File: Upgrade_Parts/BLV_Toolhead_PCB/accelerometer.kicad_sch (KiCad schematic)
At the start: 8 parts

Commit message: termination fix
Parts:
- added R?: 100, symbol Device:R
- added U?: SN65LVDS1DBV, Package_TO_SOT_SMD:SOT-23-5, symbol Interface:SN65LVDS1DBV
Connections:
- net SPI_MOSI_N: now also R?.2
- net SPI_MOSI_P: now also R?.1
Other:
- note added: "3.3V version SN65LVDS2 missing symbol"
- note added: "5V!!!"
- company: (none) -> https://github.com/Battosai42/CraftbotPlus_Upgrade
- title: (none) -> BLF Toolhaed PCB
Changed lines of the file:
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@@
 (kicad_sch (version 20211123) (generator eeschema)
   (paper "A4")
+  (title_block
+    (title "BLF Toolhaed PCB")
+    (date "2022-07-16")
+    (rev "0.1")
+    (company "https://github.com/Battosai42/CraftbotPlus_Upgrade")
+  )
   (junction (at 143.51 39.37) (diameter 0) (color 0 0 0 0)
   )
@@
   (junction (at 143.51 109.22) (diameter 0) (color 0 0 0 0)
   )
+  (junction (at 97.155 80.01) (diameter 0) (color 0 0 0 0)
+  )
   (junction (at 49.53 116.84) (diameter 0) (color 0 0 0 0)
   )
   (junction (at 223.52 76.835) (diameter 0) (color 0 0 0 0)
+  )
+  (junction (at 86.995 80.01) (diameter 0) (color 0 0 0 0)
   )
   (junction (at 228.6 76.835) (diameter 0) (color 0 0 0 0)
@@
     (stroke (width 0) (type default) (color 0 0 0 0))
   )
+  (wire (pts (xy 143.51 107.95) (xy 143.51 109.22))
+    (stroke (width 0) (type default) (color 0 0 0 0))
+  )
+  (wire (pts (xy 49.53 115.57) (xy 49.53 116.84))
+    (stroke (width 0) (type default) (color 0 0 0 0))
+  )
+  (wire (pts (xy 184.15 92.71) (xy 213.36 92.71))
+    (stroke (width 0) (type default) (color 0 0 0 0))
+  )
+  (wire (pts (xy 158.75 39.37) (xy 158.75 40.64))
+    (stroke (width 0) (type default) (color 0 0 0 0))
+  )
+  (wire (pts (xy 88.9 140.97) (xy 130.81 140.97))
+    (stroke (width 0) (type default) (color 0 0 0 0))
+  )
+  (wire (pts (xy 257.175 88.265) (xy 257.175 86.995))
+    (stroke (width 0) (type default) (color 0 0 0 0))
+  )
+  (wire (pts (xy 139.7 39.37) (xy 143.51 39.37))
+    (stroke (width 0) (type default) (color 0 0 0 0))
+  )
+  (polyline (pts (xy 76.2 133.35) (xy 31.75 133.35))
+    (stroke (width 0) (type default) (color 0 0 0 0))
+  )
+  (wire (pts (xy 143.51 109.22) (xy 128.27 109.22))
+    (stroke (width 0) (type default) (color 0 0 0 0))
+  )
+  (wire (pts (xy 54.61 115.57) (xy 54.61 116.84))
+    (stroke (width 0) (type default) (color 0 0 0 0))
+  )
+  (wire (pts (xy 223.52 76.835) (xy 223.52 80.01))
+    (stroke (width 0) (type default) (color 0 0 0 0))
+  )
+  (wire (pts (xy 143.51 38.1) (xy 143.51 39.37))
+    (stroke (width 0) (type default) (color 0 0 0 0))
+  )
+  (polyline (pts (xy 107.95 31.75) (xy 177.8 31.75))
+    (stroke (width 0) (type default) (color 0 0 0 0))
+  )
+  (wire (pts (xy 64.77 80.01) (xy 86.995 80.01))
+    (stroke (width 0) (type default) (color 0 0 0 0))
+  )
+  (wire (pts (xy 158.75 49.53) (xy 158.75 48.26))
+    (stroke (width 0) (type default) (color 0 0 0 0))
+  )
+  (wire (pts (xy 54.61 116.84) (xy 49.53 116.84))
+    (stroke (width 0) (type default) (color 0 0 0 0))
+  )
+  (wire (pts (xy 64.77 87.63) (xy 97.155 87.63))
+    (stroke (width 0) (type default) (color 0 0 0 0))
+  )
+  (wire (pts (xy 184.15 58.42) (xy 184.15 92.71))
+    (stroke (width 0) (type default) (color 0 0 0 0))
+  )
   (wire (pts (xy 88.9 100.33) (xy 88.9 140.97))
     (stroke (width 0) (type default) (color 0 0 0 0))
   )
-  (wire (pts (xy 143.51 107.95) (xy 143.51 109.22))
-    (stroke (width 0) (type default) (color 0 0 0 0))
-  )
-  (wire (pts (xy 49.53 115.57) (xy 49.53 116.84))
-    (stroke (width 0) (type default) (color 0 0 0 0))
-  )
-  (wire (pts (xy 184.15 92.71) (xy 213.36 92.71))
-    (stroke (width 0) (type default) (color 0 0 0 0))
-  )
-  (wire (pts (xy 158.75 39.37) (xy 158.75 40.64))
-    (stroke (width 0) (type default) (color 0 0 0 0))
-  )
-  (wire (pts (xy 88.9 140.97) (xy 130.81 140.97))
-    (stroke (width 0) (type default) (color 0 0 0 0))
-  )
-  (wire (pts (xy 257.175 88.265) (xy 257.175 86.995))
-    (stroke (width 0) (type default) (color 0 0 0 0))
-  )
-  (wire (pts (xy 139.7 39.37) (xy 143.51 39.37))
-    (stroke (width 0) (type default) (color 0 0 0 0))
-  )
-  (polyline (pts (xy 76.2 133.35) (xy 31.75 133.35))
-    (stroke (width 0) (type default) (color 0 0 0 0))
-  )
-  (wire (pts (xy 143.51 109.22) (xy 128.27 109.22))
-    (stroke (width 0) (type default) (color 0 0 0 0))
-  )
-  (wire (pts (xy 54.61 115.57) (xy 54.61 116.84))
-    (stroke (width 0) (type default) (color 0 0 0 0))
-  )
-  (wire (pts (xy 223.52 76.835) (xy 223.52 80.01))
-    (stroke (width 0) (type default) (color 0 0 0 0))
-  )
-  (wire (pts (xy 143.51 38.1) (xy 143.51 39.37))
-    (stroke (width 0) (type default) (color 0 0 0 0))
-  )
-  (polyline (pts (xy 107.95 31.75) (xy 177.8 31.75))
-    (stroke (width 0) (type default) (color 0 0 0 0))
-  )
-  (wire (pts (xy 64.77 80.01) (xy 95.25 80.01))
-    (stroke (width 0) (type default) (color 0 0 0 0))
-  )
-  (wire (pts (xy 158.75 49.53) (xy 158.75 48.26))
-    (stroke (width 0) (type default) (color 0 0 0 0))
-  )
-  (wire (pts (xy 54.61 116.84) (xy 49.53 116.84))
-    (stroke (width 0) (type default) (color 0 0 0 0))
-  )
-  (wire (pts (xy 64.77 87.63) (xy 97.155 87.63))
-    (stroke (width 0) (type default) (color 0 0 0 0))
-  )
-  (wire (pts (xy 184.15 58.42) (xy 184.15 92.71))
-    (stroke (width 0) (type default) (color 0 0 0 0))
-  )
   (wire (pts (xy 64.77 77.47) (xy 66.04 77.47))
     (stroke (width 0) (type default) (color 0 0 0 0))
@@
     (stroke (width 0) (type default) (color 0 0 0 0))
   )
-  (wire (pts (xy 95.25 55.88) (xy 130.81 55.88))
+  (wire (pts (xy 86.995 55.88) (xy 130.81 55.88))
     (stroke (width 0) (type default) (color 0 0 0 0))
   )
@@
     (stroke (width 0) (type default) (color 0 0 0 0))
   )
-  (wire (pts (xy 97.155 85.09) (xy 97.155 60.96))
+  (wire (pts (xy 86.995 55.88) (xy 86.995 80.01))
+    (stroke (width 0) (type default) (color 0 0 0 0))
+  )
+  (wire (pts (xy 97.155 85.09) (xy 97.155 80.01))
     (stroke (width 0) (type default) (color 0 0 0 0))
   )
@@
     (stroke (width 0) (type default) (color 0 0 0 0))
   )
+  (wire (pts (xy 97.155 60.96) (xy 97.155 80.01))
+    (stroke (width 0) (type default) (color 0 0 0 0))
+  )
   (polyline (pts (xy 267.335 120.65) (xy 196.85 120.65))
     (stroke (width 0) (type default) (color 0 0 0 0))
@@
     (stroke (width 0) (type default) (color 0 0 0 0))
   )
+  (wire (pts (xy 95.885 80.01) (xy 97.155 80.01))
+    (stroke (width 0) (type default) (color 0 0 0 0))
+  )
   (wire (pts (xy 90.805 95.25) (xy 90.805 135.89))
     (stroke (width 0) (type default) (color 0 0 0 0))
@@
     (stroke (width 0) (type default) (color 0 0 0 0))
   )
-  (wire (pts (xy 95.25 80.01) (xy 95.25 55.88))
-    (stroke (width 0) (type default) (color 0 0 0 0))
-  )
   (wire (pts (xy 184.15 95.25) (xy 213.36 95.25))
     (stroke (width 0) (type default) (color 0 0 0 0))
@@
   )
   (polyline (pts (xy 267.335 69.85) (xy 267.335 120.65))
+    (stroke (width 0) (type default) (color 0 0 0 0))
+  )
+  (wire (pts (xy 86.995 80.01) (xy 88.265 80.01))
     (stroke (width 0) (type default) (color 0 0 0 0))
   )
@@
     (effects (font (size 2 2) (thickness 0.4) bold) (justify left bottom))
   )
+  (text "5V!!!" (at 147.955 54.61 0)
+    (effects (font (size 1.27 1.27)) (justify left bottom))
+  )
+  (text "3.3V version\nSN65LVDS2 missing symbol" (at 219.075 50.165 0)
+    (effects (font (size 1.27 1.27)) (justify left bottom))
+  )
   (text "RJ45 Connector" (at 33.02 132.08 0)
     (effects (font (size 2 2) (thickness 0.4) bold) (justify left bottom))
@@
   (text "LVDS Interface" (at 109.22 157.48 0)
     (effects (font (size 2 2) (thickness 0.4) bold) (justify left bottom))
+  )
+  (text "5V!!!" (at 148.59 123.825 0)
+    (effects (font (size 1.27 1.27)) (justify left bottom))
   )
   (text "Data lines are routed as differential lines to reduce interferance"
@@
     (pin "SH")
   )
+  (symbol (lib_id "Interface:SN65LVDS1DBV") (at 216.535 37.465 0) (unit 1)
+    (in_bom yes) (on_board yes) (fields_autoplaced)
+    (property "Reference" "U?" (id 0) (at 218.5544 24.13 0)
+      (effects (font (size 1.27 1.27)) (justify left))
+    )
+    (property "Value" "SN65LVDS1DBV" (id 1) (at 218.5544 26.67 0)
+      (effects (font (size 1.27 1.27)) (justify left))
+    )
+    (property "Footprint" "Package_TO_SOT_SMD:SOT-23-5" (id 2) (at 216.535 48.895 0)
+      (effects (font (size 1.27 1.27)) hide)
+    )
+    (property "Datasheet" "http://www.ti.com/lit/ds/symlink/sn65lvds1.pdf" (id 3) (at 216.535 34.925 0)
+      (effects (font (size 1.27 1.27)) hide)
+    )
+    (pin "1")
+    (pin "2")
+    (pin "3")
+    (pin "4")
+    (pin "5")
+  )
   (symbol (lib_id "Interface:DS90C402") (at 143.51 63.5 0) (unit 1)
     (in_bom yes) (on_board yes)
@@
     (pin "1")
   )
+  (symbol (lib_id "Device:R") (at 92.075 80.01 90) (unit 1)
+    (in_bom yes) (on_board yes)
+    (property "Reference" "R?" (id 0) (at 92.075 78.105 90))
+    (property "Value" "100" (id 1) (at 92.075 81.915 90))
+    (property "Footprint" "" (id 2) (at 92.075 81.788 90)
+      (effects (font (size 1.27 1.27)) hide)
+    )
+    (property "Datasheet" "~" (id 3) (at 92.075 80.01 0)
+      (effects (font (size 1.27 1.27)) hide)
+    )
+    (pin "1")
+    (pin "2")
+  )
   (symbol (lib_id "power:+3.3V") (at 143.51 38.1 0) (unit 1)

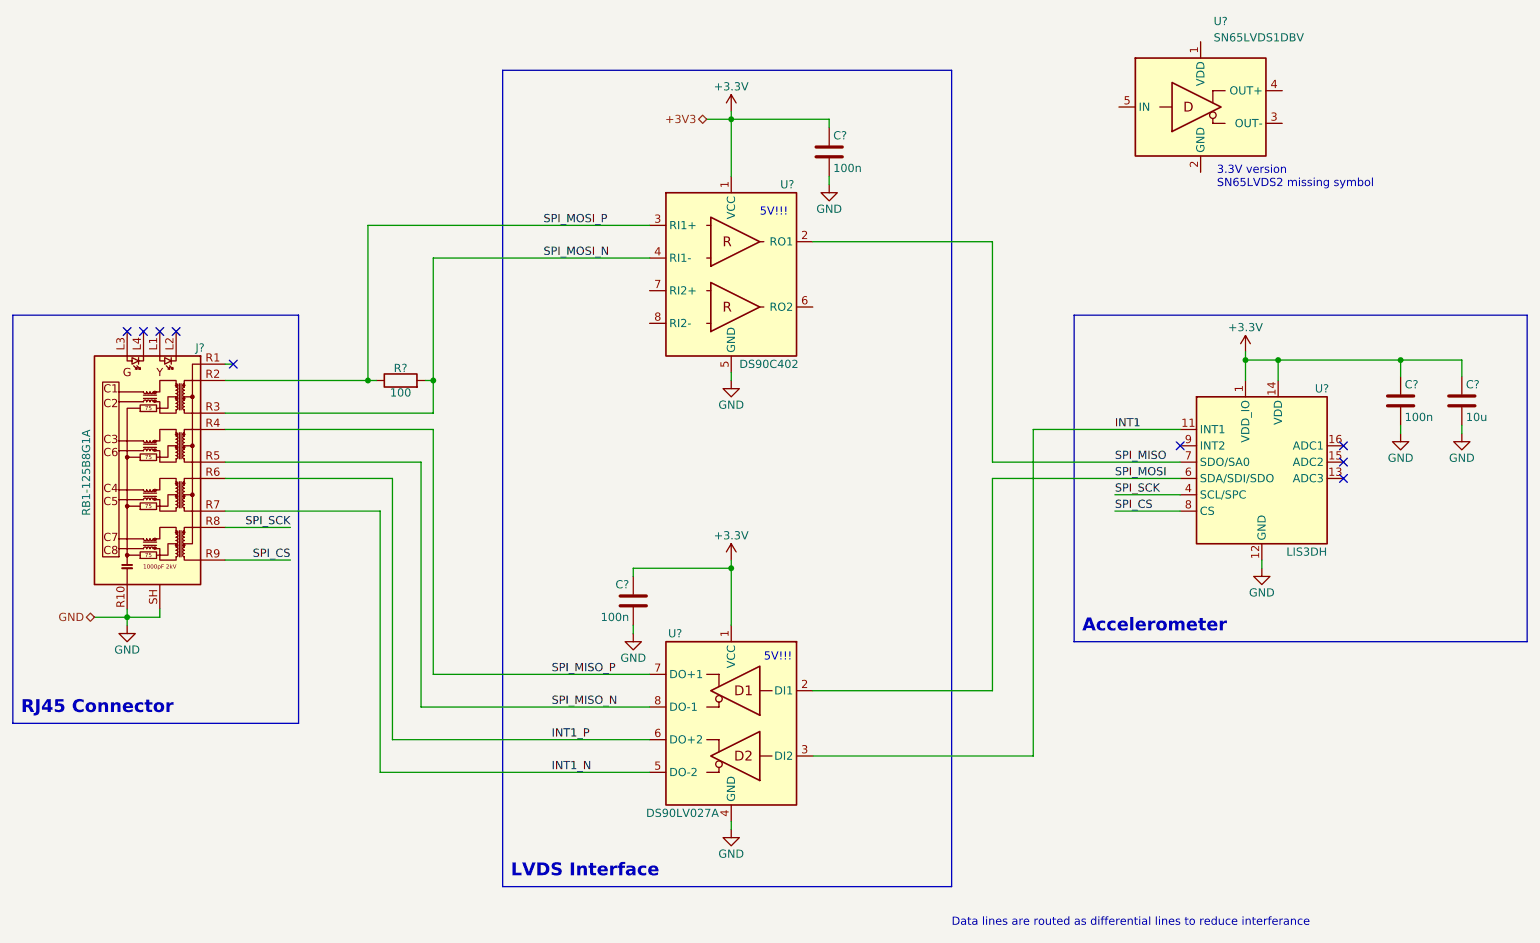
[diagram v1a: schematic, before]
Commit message: using 3.3V LVDS driver
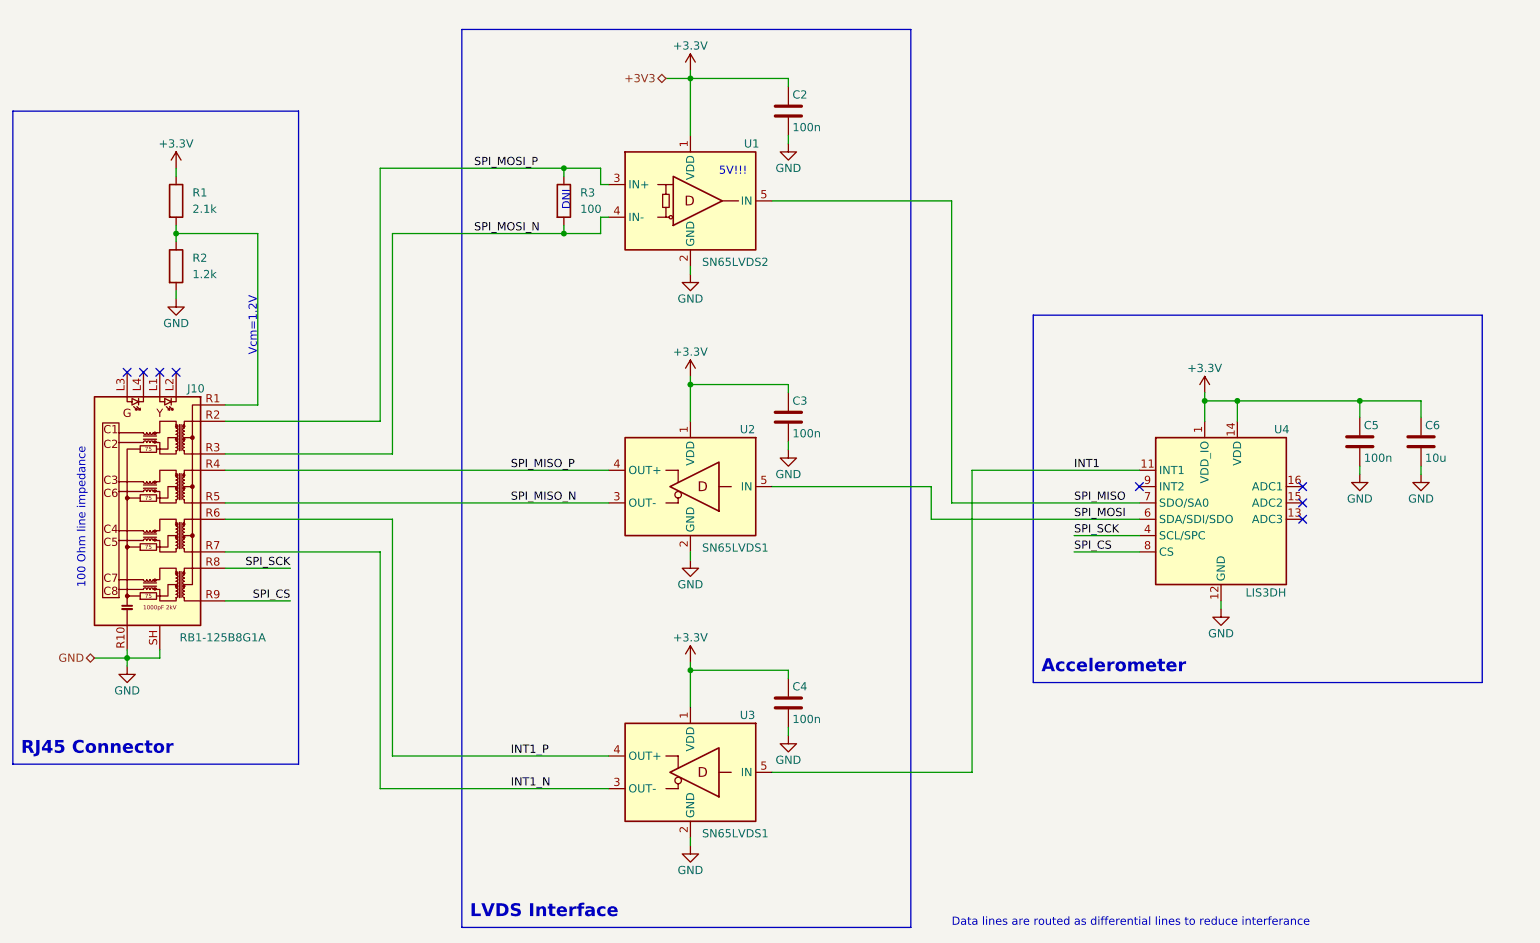
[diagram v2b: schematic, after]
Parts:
- removed C?: 100n, symbol Device:C
- removed R?: 100, symbol Device:R
- removed U?: SN65LVDS1DBV, Package_TO_SOT_SMD:SOT-23-5, symbol Interface:SN65LVDS1DBV
- removed U?: DS90C402, Package_SO:SOIC-8_3.9x4.9mm_P1.27mm, symbol Interface:DS90C402
- removed U?: DS90LV027A, Package_SO:SOIC-8_3.9x4.9mm_P1.27mm, symbol Interface:DS90LV027A
- added C3, C4: 100n, symbol Device:C
- added R1: 2.1k, symbol Device:R
- added R2: 1.2k, symbol Device:R
- added R3: 100, symbol Device:R
- added U1: SN65LVDS2, Package_TO_SOT_SMD:SOT-23-5, symbol toolhead:SN65LVDS2
- added U2, U3: SN65LVDS1, Package_TO_SOT_SMD:SOT-23-5, symbol toolhead:SN65LVDS1
- gave numbers to parts that had none: 5
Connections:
- net +3V3: now also C3.1, C4.1, R1.1, U1.1 (VDD), U2.1 (VDD), U3.1 (VDD)
- net GND: now also C3.2, C4.2, R2.2, U1.2 (GND), U2.2 (GND), U3.2 (GND)
- net INT1: now also U3.5 (IN)
- net INT1_N: now also U3.3 (OUT-)
- net INT1_P: now also U3.4 (OUT+)
- net SPI_MISO: now also U1.5 (IN)
- net SPI_MISO_N: now also U2.3 (OUT-)
- net SPI_MISO_P: now also U2.4 (OUT+)
- net SPI_MOSI: now also U2.5 (IN)
- net SPI_MOSI_N: now also R3.2, U1.4 (IN-)
- net SPI_MOSI_P: now also R3.1, U1.3 (IN+)
- net at J10.R1 (CT): now also R1.2, R2.1
- no-connect marks 9 -> 8
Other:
- note added: "100 Ohm line impedance"
- note added: "DNI"
- note added: "Vcm=1.2V"
- note removed: "3.3V version SN65LVDS2 missing symbol"
- moved on the sheet: C2, C5, C6, J10, U4
